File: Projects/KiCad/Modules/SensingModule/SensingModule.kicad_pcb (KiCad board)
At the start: 2 copper layers, 110 x 95 mm, 46 parts, among them J1 Conn_01x02, J2 Conn_01x08, J3 Conn_01x02_Pin, J4 Micro_SD_Card_Det_Hirose_DM3AT, SW1 SW_DIP_x02, U1 MCP2562-E-P, U4 TLP222A, U5 NUCLEO-F303K8, U6 MB85RS2MT, U7 MB85RS2MT

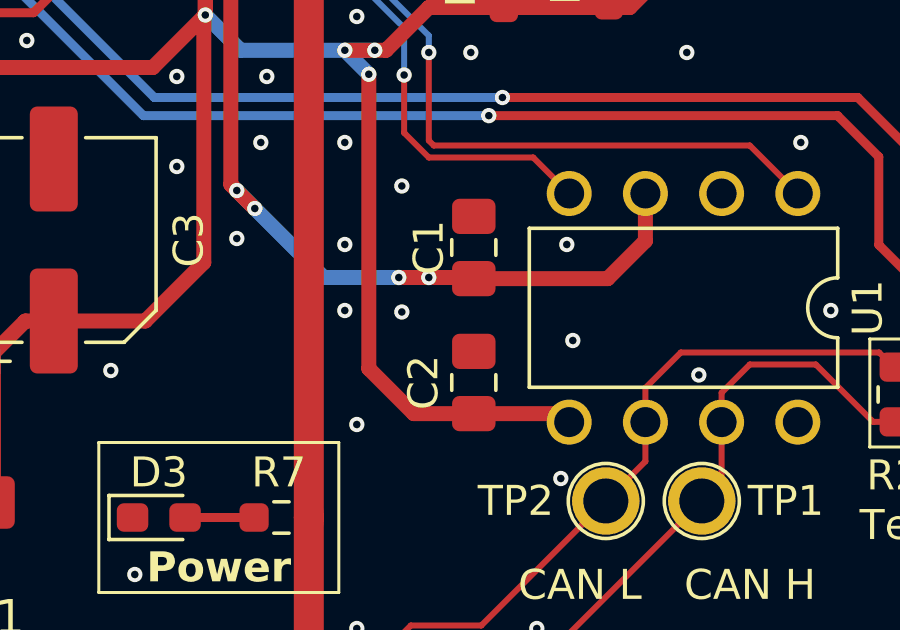
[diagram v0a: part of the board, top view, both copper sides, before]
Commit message: チップ積層セラミックコンデンサをSMD1608に変更
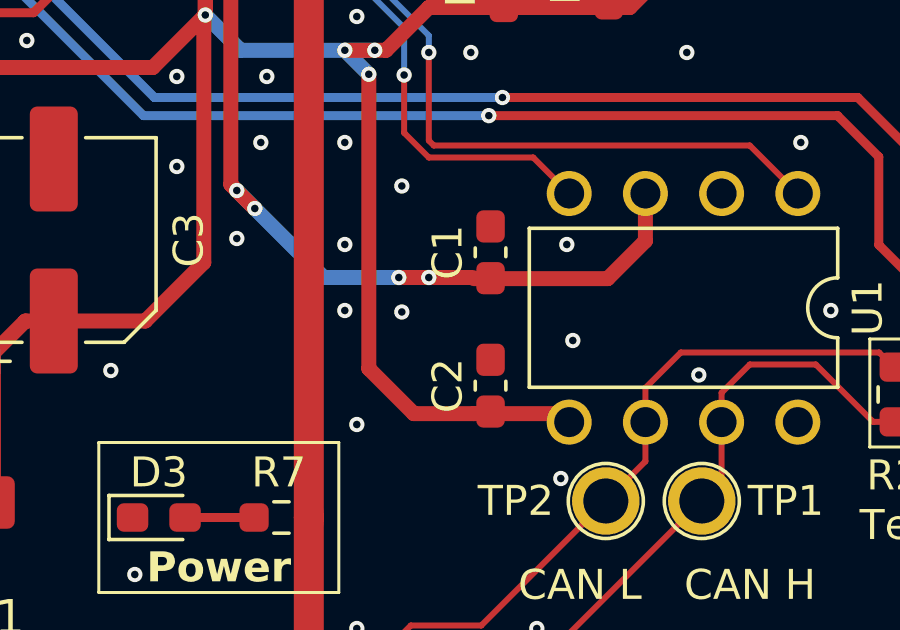
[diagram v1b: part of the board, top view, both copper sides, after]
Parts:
- C1, C2: footprint Capacitor_SMD:C_0805_2012Metric_Pad1.18x1.45mm_HandSolder -> Capacitor_SMD:C_0603_1608Metric_Pad1.08x0.95mm_HandSolder
- moved C1 0.58 mm to (168.1, 116.7)
- moved C2 0.57 mm to (168.1, 121.1)

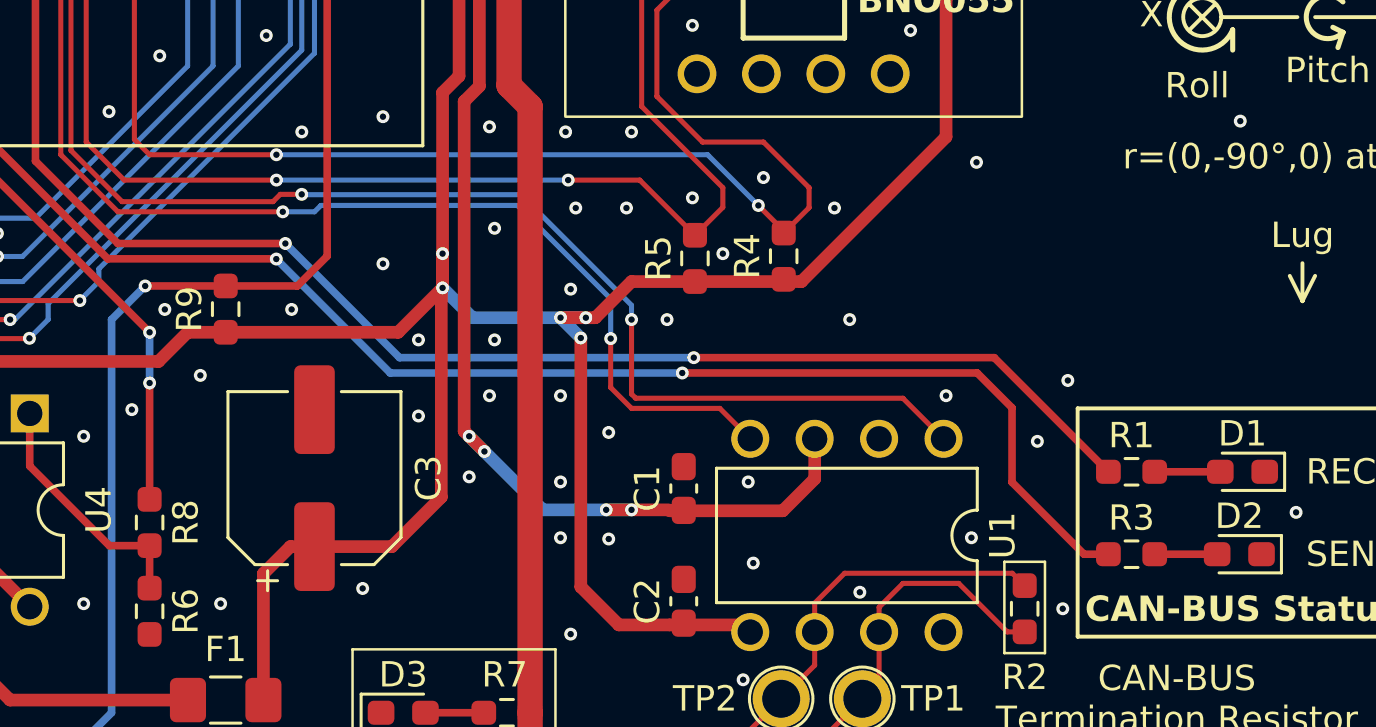
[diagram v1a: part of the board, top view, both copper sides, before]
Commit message: 抵抗の在庫に合わせてサイズを変更
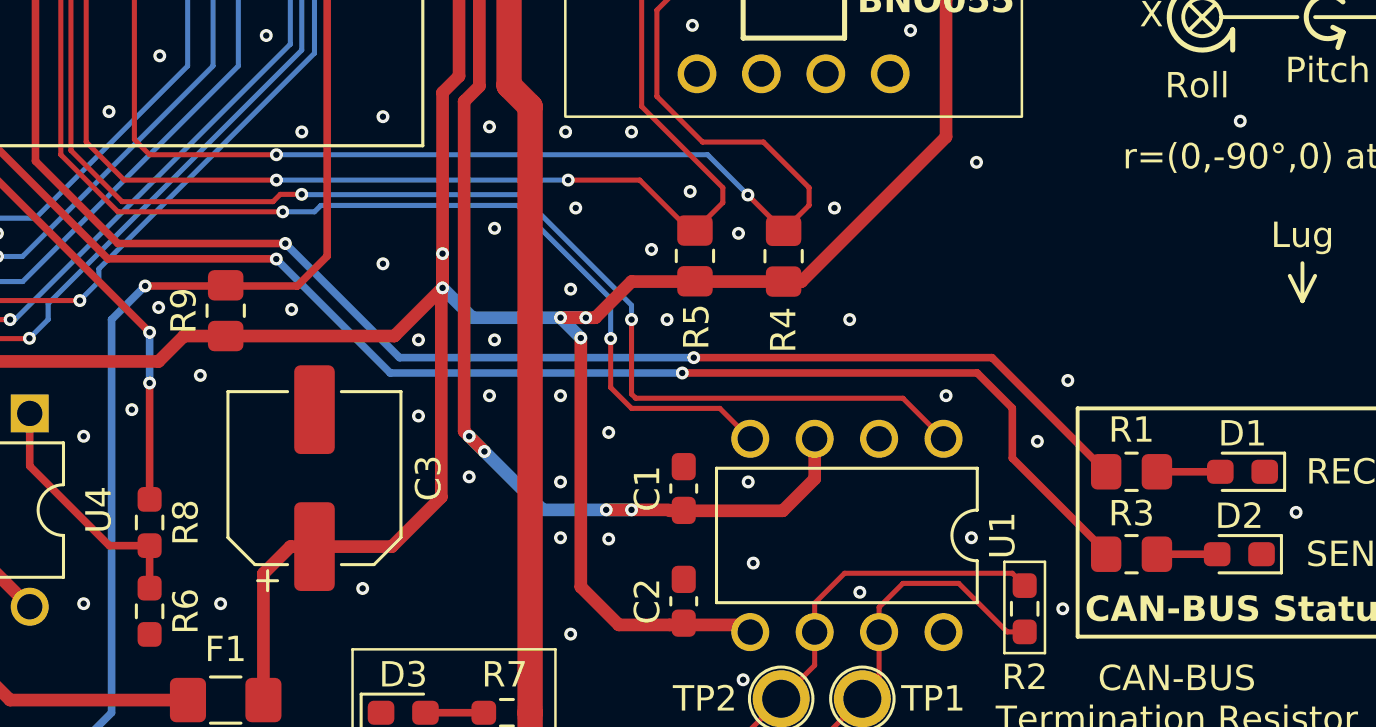
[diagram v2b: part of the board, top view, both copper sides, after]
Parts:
- R1, R3, R4, R5, R9: footprint Resistor_SMD:R_0603_1608Metric_Pad0.98x0.95mm_HandSolder -> Resistor_SMD:R_0805_2012Metric_Pad1.20x1.40mm_HandSolder
- moved R5 0.10 mm to (168.5, 107.5)
- moved R9 0.06 mm to (150.0, 109.6)
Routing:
- net CAN_SEND_STATUS: track 59.7 -> 59.1 mm
- net GND: vias 171 -> 170

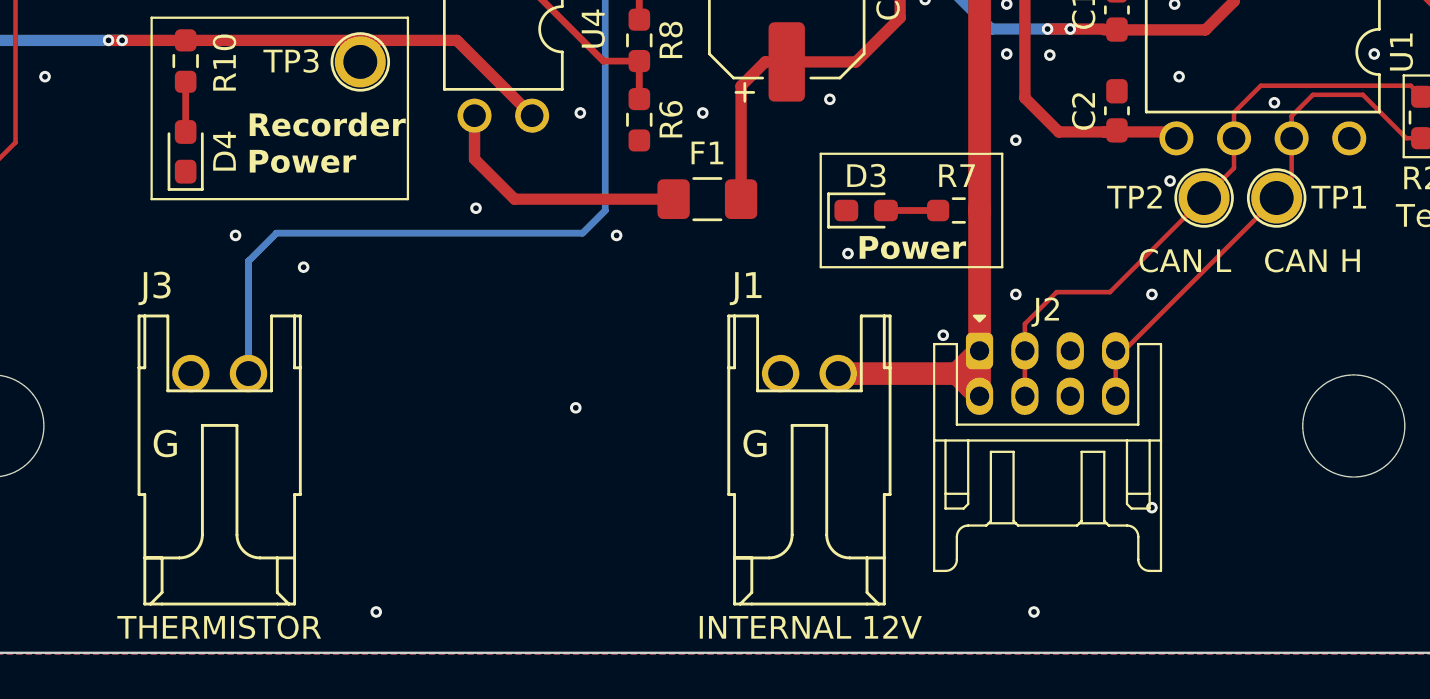
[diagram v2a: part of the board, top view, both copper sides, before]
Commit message: コネクタ位置を揃えた
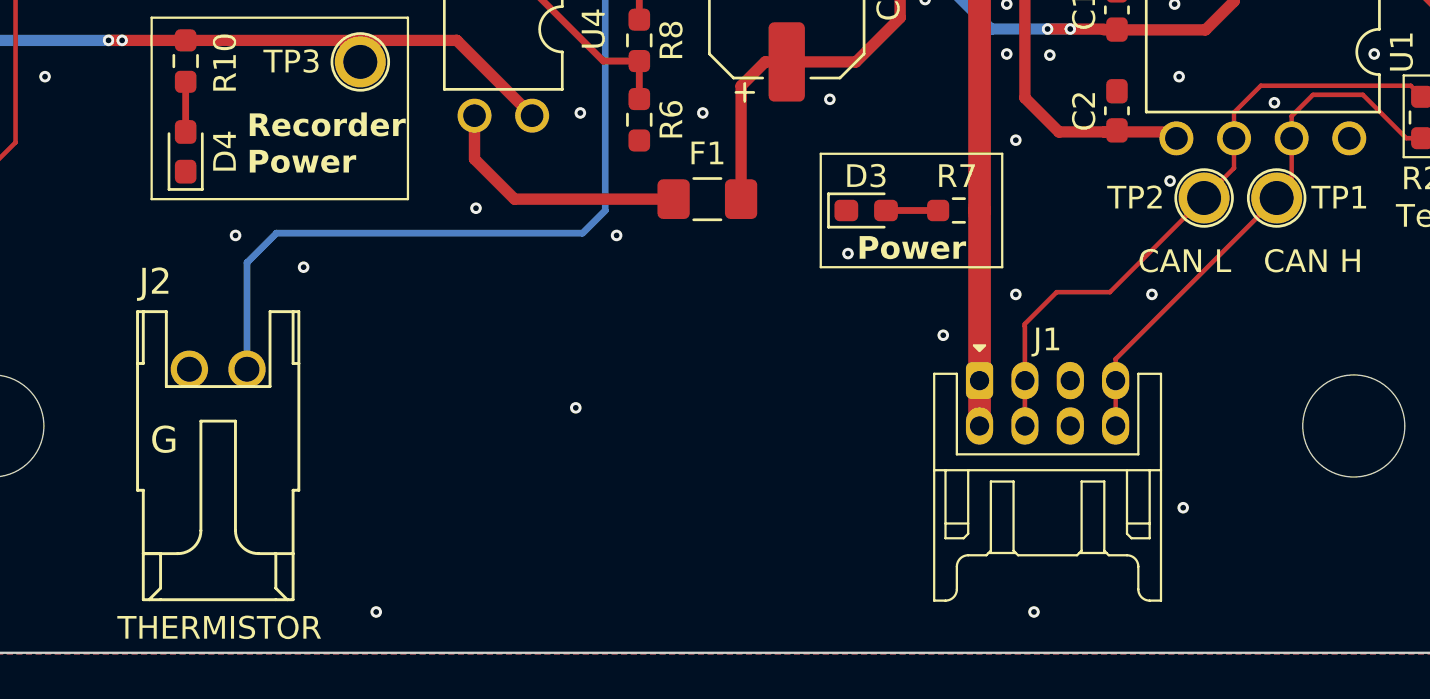
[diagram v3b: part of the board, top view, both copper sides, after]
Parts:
- removed the J1 at (153.2, 132.7)
- moved J1 1.31 mm to (162.0, 133.0)
- moved J2 0.20 mm to (127.2, 132.5)
- renumbered J2 to J1, J3 to J2
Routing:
- net +12V: track 84.7 -> 77.9 mm
- net CAN_H: track 22.3 -> 23.8 mm
- net CAN_L: track 26.7 -> 28.0 mm
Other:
- board text removed: "INTERNAL 12V"

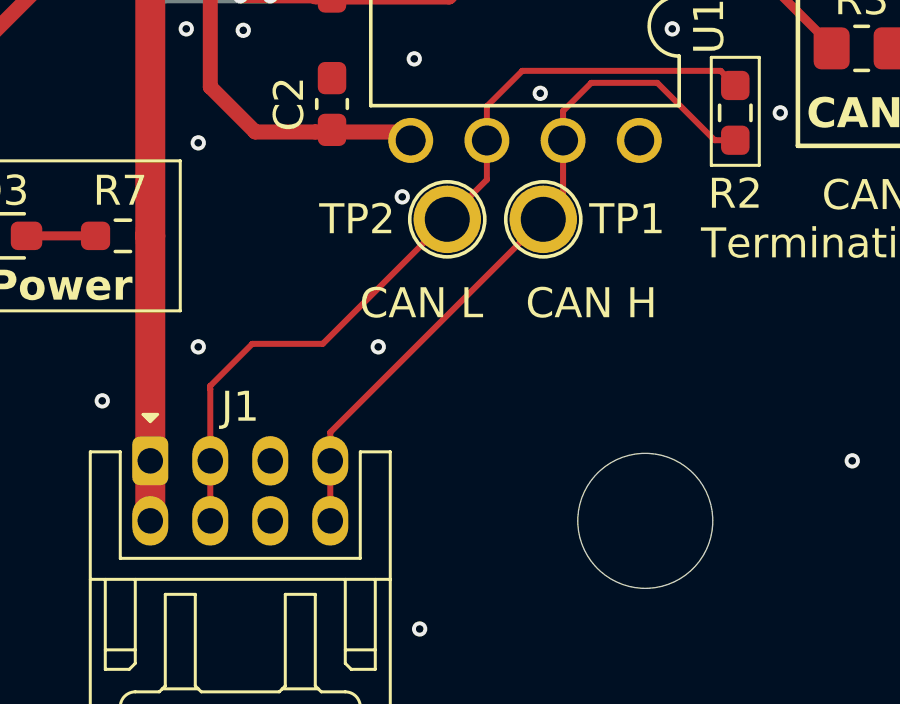
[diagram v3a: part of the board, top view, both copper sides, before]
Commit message: コネクタのピン配置を変更
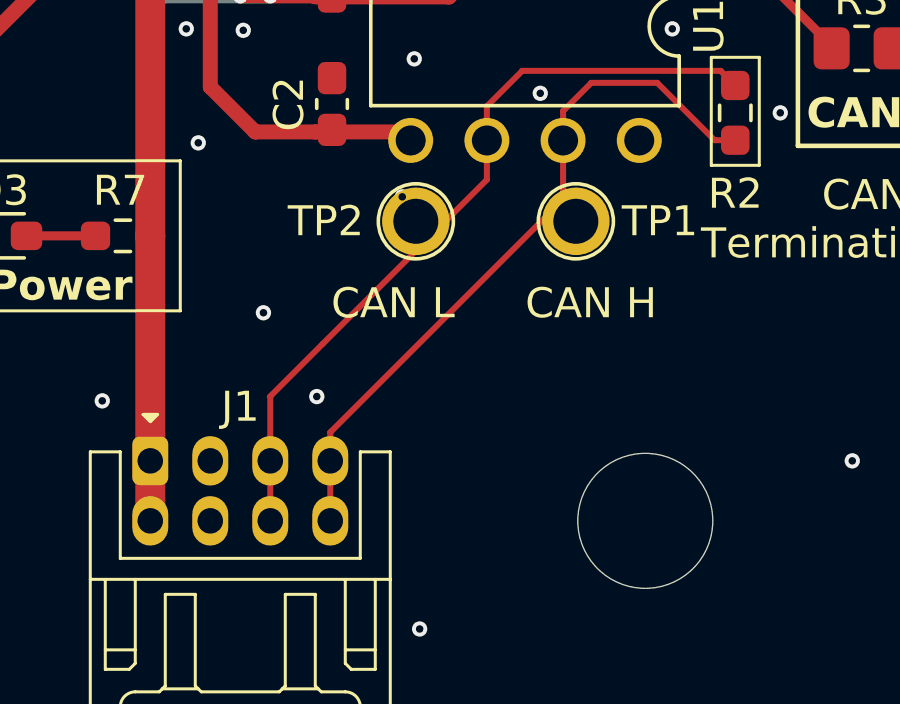
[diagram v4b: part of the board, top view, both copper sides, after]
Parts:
- moved TP1 1.09 mm to (176.2, 125.0)
- moved TP2 1.05 mm to (170.9, 125.0)
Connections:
- J1 pad 3: CAN_L -> GND
- J1 pad 4: CAN_L -> GND
- J1 pad 5: GND -> CAN_L
- J1 pad 6: GND -> CAN_L
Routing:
- net CAN_L: track 28.0 -> 25.8 mm

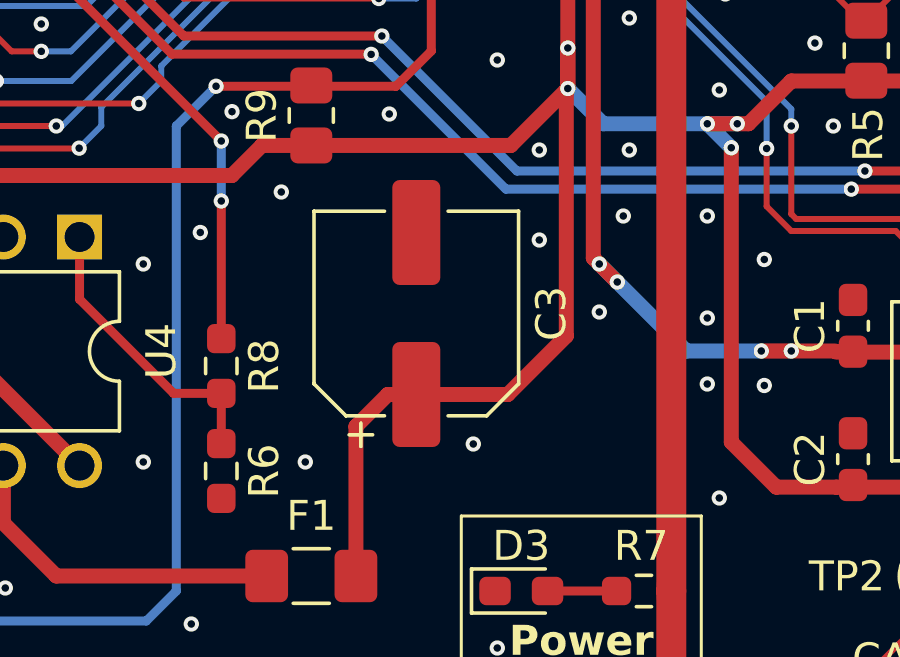
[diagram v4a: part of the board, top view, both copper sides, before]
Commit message: バッファコンデンサを表面実装に変更
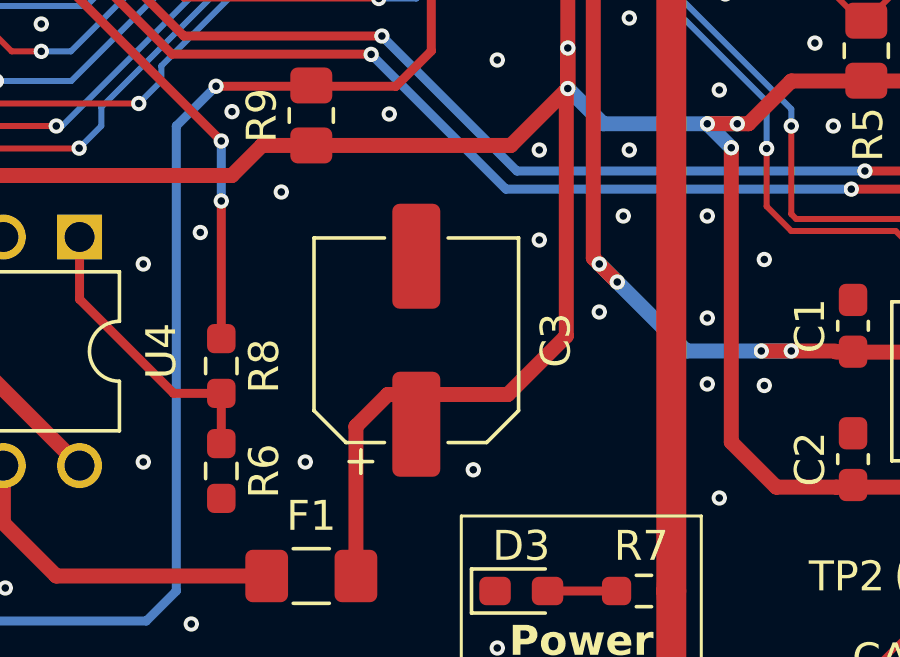
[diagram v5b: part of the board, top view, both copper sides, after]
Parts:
- C3: value 100μF -> 47μF; footprint Capacitor_SMD:CP_Elec_6.3x7.7 -> Capacitor_SMD:CP_Elec_6.3x5.9
- moved C3 0.89 mm to (153.5, 117.1)
